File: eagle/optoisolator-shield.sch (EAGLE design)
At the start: 48 parts, among them Q1 MMBT2222ALT3G, Q2 MMBT2222ALT3G, Q3 MMBT2222ALT3G, Q4 MMBT2222ALT3G, Q5 MMBT2222ALT3G, Q6 MMBT2222ALT3G, U1 OPTO, U2 OPTO, U3 OPTO

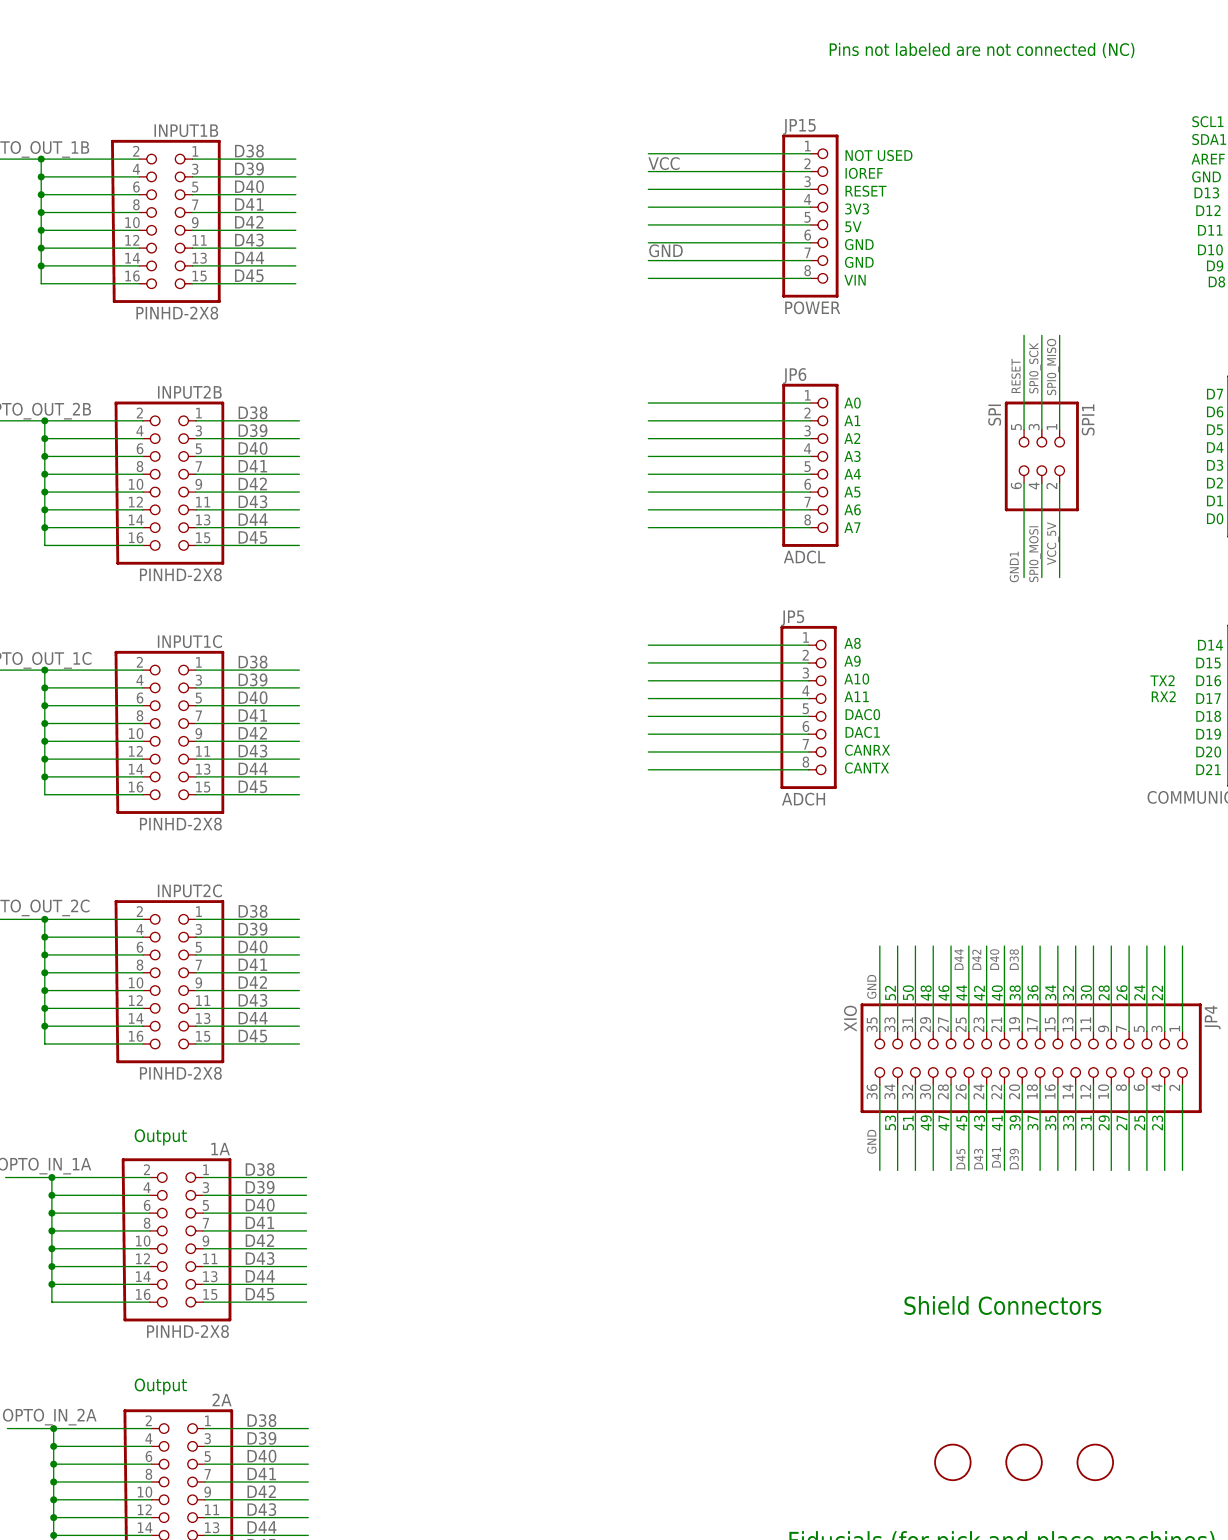
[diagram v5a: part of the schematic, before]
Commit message: improved trace clearances; changed names of inputs from 1A... to A1... for better readability
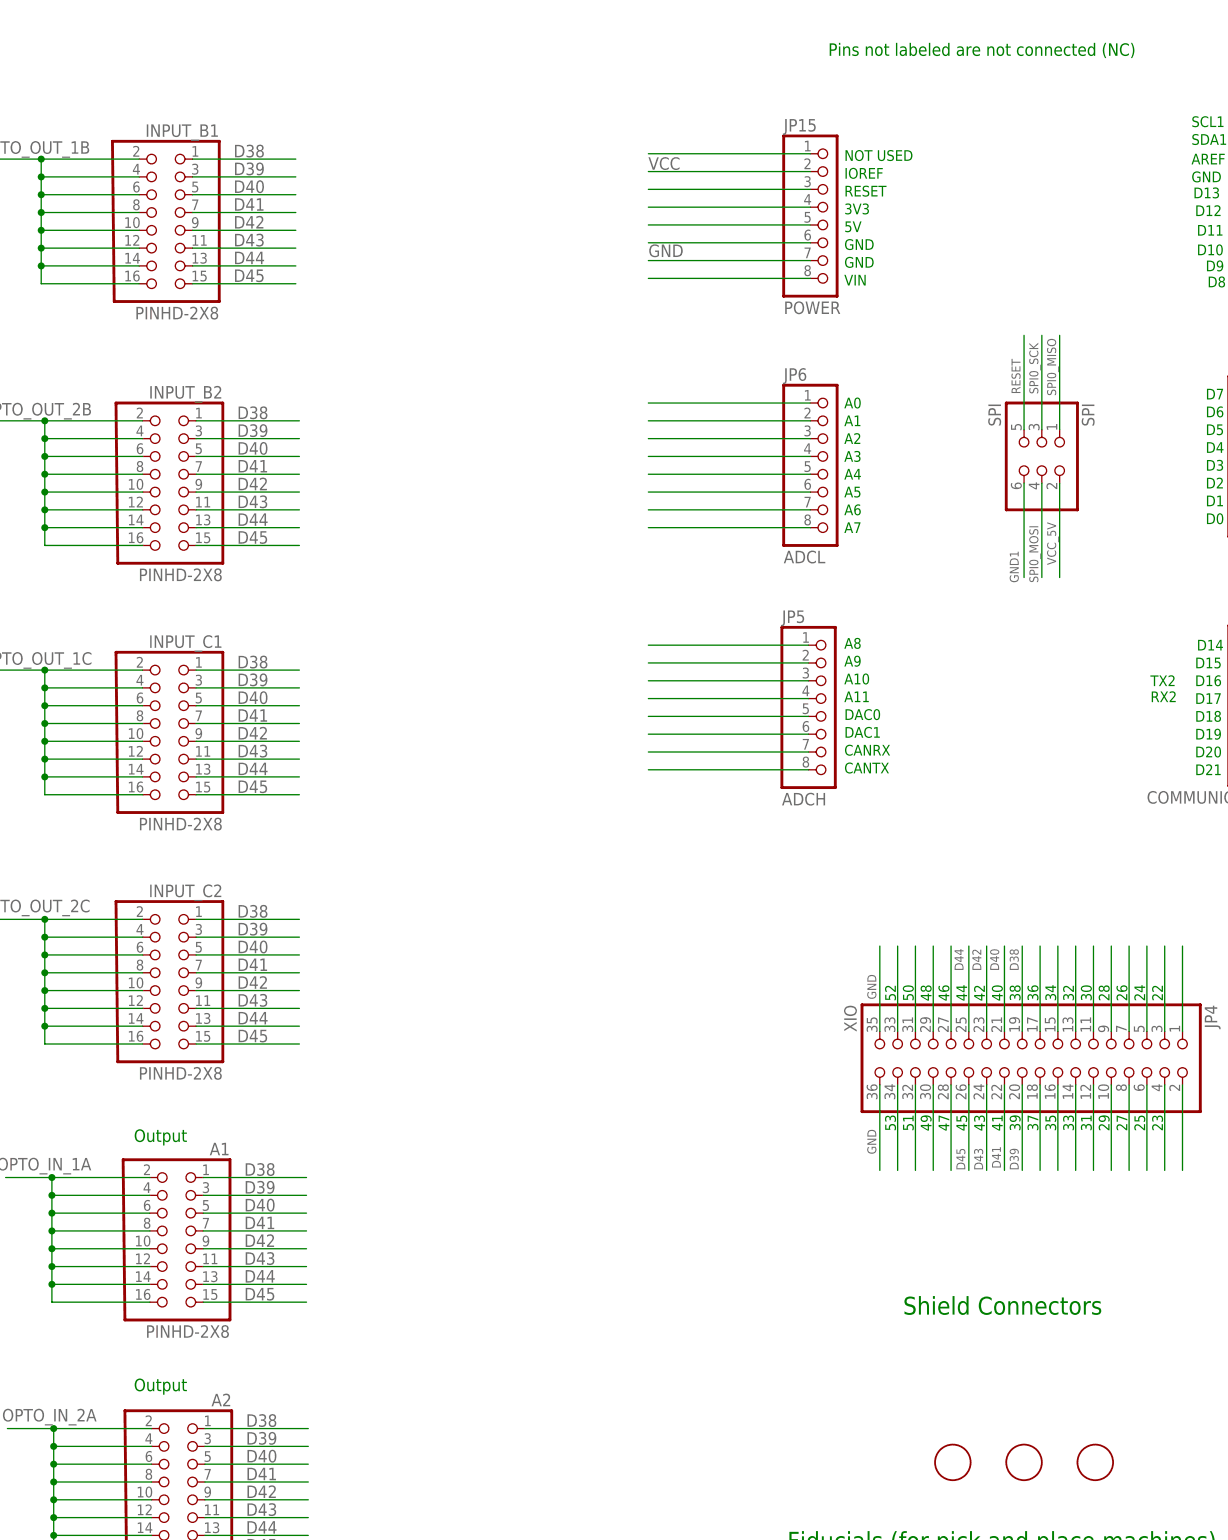
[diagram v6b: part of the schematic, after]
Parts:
- renumbered 1A to A1, 2A to A2, INPUT1B to INPUT_B1, INPUT1C to INPUT_C1, INPUT2B to INPUT_B2, INPUT2C to INPUT_C2, SPI1 to SPI
